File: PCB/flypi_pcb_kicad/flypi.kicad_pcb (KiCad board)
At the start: 2 copper layers, 76 x 93 mm, 44 parts, among them CON1 BARREL_JACK, P1 PeltS1S2, P10 RGB RG-B, P2 Pi+-, P3 Fan-+, P4 Therm +s-, P5 HP1-+, P6 HP2-+, P7 servo -s+, P8 Ring s-+, P9 matrix sdsc-+, Q1 1A_NPN_ECB, Q2 1A-NPN-ECB, Q3 1A_NPN_ECB, Q4 1A_NPN_ECB, U1 LM2596, U2 LM2596, U3 LM2596, U4 L298N, U5 arduino_mini

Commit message: same here.
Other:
- board text added: "Fly pi rev. 0.3 20170730"
- board text removed: "Fly pi rev. 0.2 20160726"
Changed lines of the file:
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@@
-(kicad_pcb (version 4) (host pcbnew 4.0.2+e4-6225~38~ubuntu14.04.1-stable)
+(kicad_pcb (version 4) (host pcbnew 4.0.6-e0-6349~53~ubuntu16.04.1)
   (general
     (links 94)
     (no_connects 3)
-    (area 102.4 38.4 187.7 136.55)
+    (area 102.4 38.4 187.55 136.55)
     (thickness 1.6)
     (drawings 11)
@@
       (excludeedgelayer true)
       (linewidth 0.100000)
-      (plotframeref false)
+      (plotframeref true)
       (viasonmask false)
       (mode 1)
@@
       (plotvalue true)
       (plotinvisibletext false)
-      (padsonsilk false)
+      (padsonsilk true)
       (subtractmaskfromsilk false)
       (outputformat 1)
@@
   (target plus (at 104.95 134.05) (size 5) (width 0.1) (layer Edge.Cuts))
   (target plus (at 181.05 134.05) (size 5) (width 0.1) (layer Edge.Cuts))
-  (gr_text "Fly pi rev. 0.2 20160726\n\n" (at 145.05 131.95) (layer F.SilkS)
+  (gr_text "Fly pi rev. 0.3 20170730\n\n" (at 145.05 131.95) (layer F.SilkS)
     (effects (font (size 1.5 1.5) (thickness 0.3)))
   )
@@
   (segment (start 116.16 76.84) (end 114.25 78.75) (width 0.5) (layer F.Cu) (net 2))
   (segment (start 113 87.5) (end 112 87.5) (width 0.5) (layer F.Cu) (net 2))
-  (segment (start 163 65) (end 163.25 65) (width 1) (layer B.Cu) (net 3) (status C00000))
-  (segment (start 163.25 65) (end 164.675 66.425) (width 1) (layer B.Cu) (net 3) (status 400000))
-  (segment (start 169.2 66.425) (end 171.725 63.9) (width 1) (layer B.Cu) (net 3) (status 800000))
+  (segment (start 163 65) (end 163.25 65) (width 1) (layer B.Cu) (net 3))
+  (segment (start 163.25 65) (end 164.675 66.425) (width 1) (layer B.Cu) (net 3))
+  (segment (start 169.2 66.425) (end 171.725 63.9) (width 1) (layer B.Cu) (net 3))
   (segment (start 164.675 66.425) (end 169.2 66.425) (width 1) (layer B.Cu) (net 3))
   (segment (start 171.775 62.925) (end 171.65 62.925) (width 1) (layer F.Cu) (net 3))
@@
   (segment (start 121 64.49936) (end 129.50064 64.49936) (width 1) (layer B.Cu) (net 4))
   (segment (start 129.50064 64.49936) (end 136 58) (width 1) (layer B.Cu) (net 4))
-  (segment (start 175.925 69) (end 175.925 68.725) (width 1) (layer F.Cu) (net 5) (status C00000))
-  (segment (start 175.925 68.725) (end 178.425 66.225) (width 1) (layer F.Cu) (net 5) (status 400000))
+  (segment (start 175.925 69) (end 175.925 68.725) (width 1) (layer F.Cu) (net 5))
+  (segment (start 175.925 68.725) (end 178.425 66.225) (width 1) (layer F.Cu) (net 5))
   (segment (start 173.4 52.35) (end 173.025 51.975) (width 1) (layer F.Cu) (net 5))
   (segment (start 176.65 52.35) (end 173.4 52.35) (width 1) (layer F.Cu) (net 5))
   (segment (start 178.425 54.125) (end 176.65 52.35) (width 1) (layer F.Cu) (net 5))
   (segment (start 178.425 66.225) (end 178.425 54.125) (width 1) (layer F.Cu) (net 5))
-  (segment (start 175.925 69) (end 175.925 75.25) (width 1) (layer F.Cu) (net 5) (status 400000))
+  (segment (start 175.925 69) (end 175.925 75.25) (width 1) (layer F.Cu) (net 5))
   (segment (start 175.925 75.25) (end 173.05 78.125) (width 1) (layer F.Cu) (net 5))
   (segment (start 173.1 79.125) (end 173.1 78.475) (width 1) (layer B.Cu) (net 5))

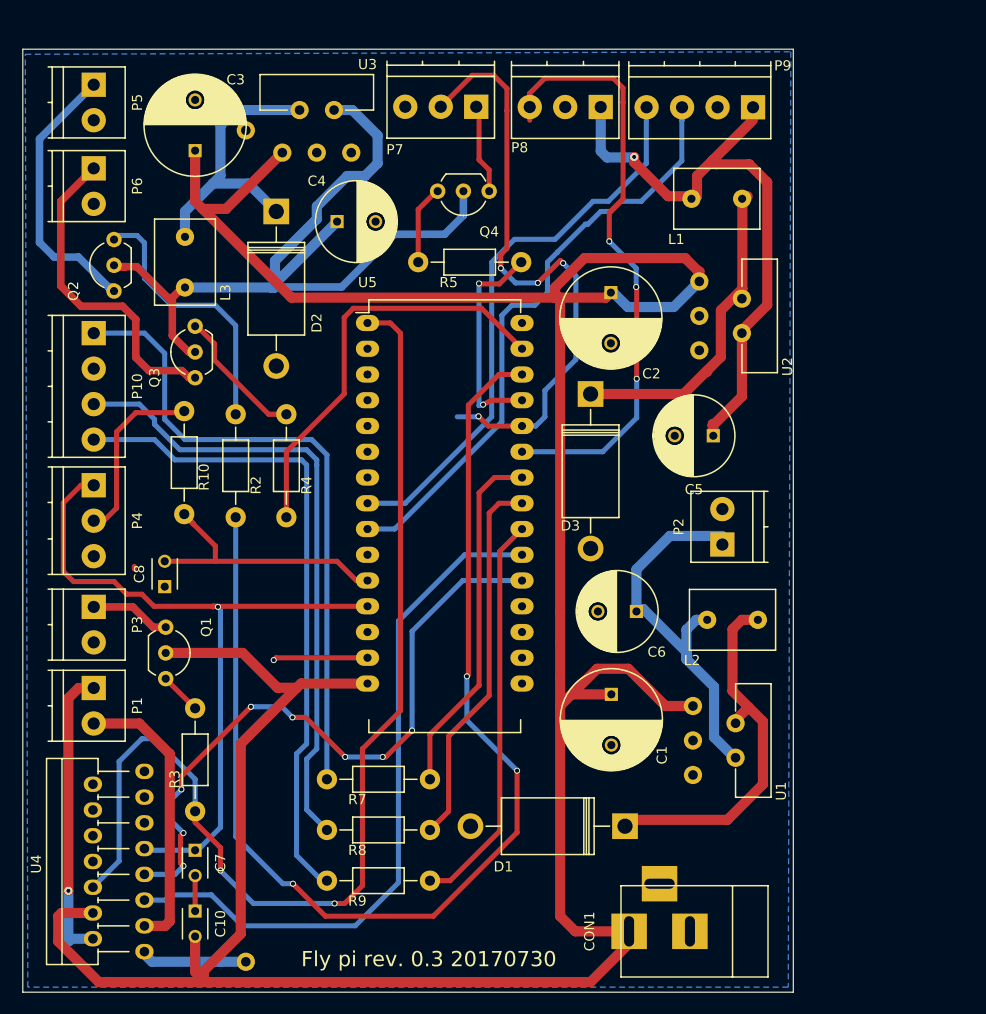
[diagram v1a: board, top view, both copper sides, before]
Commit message: update to pcbs. Both SMD and new through hole. PCB is untested.
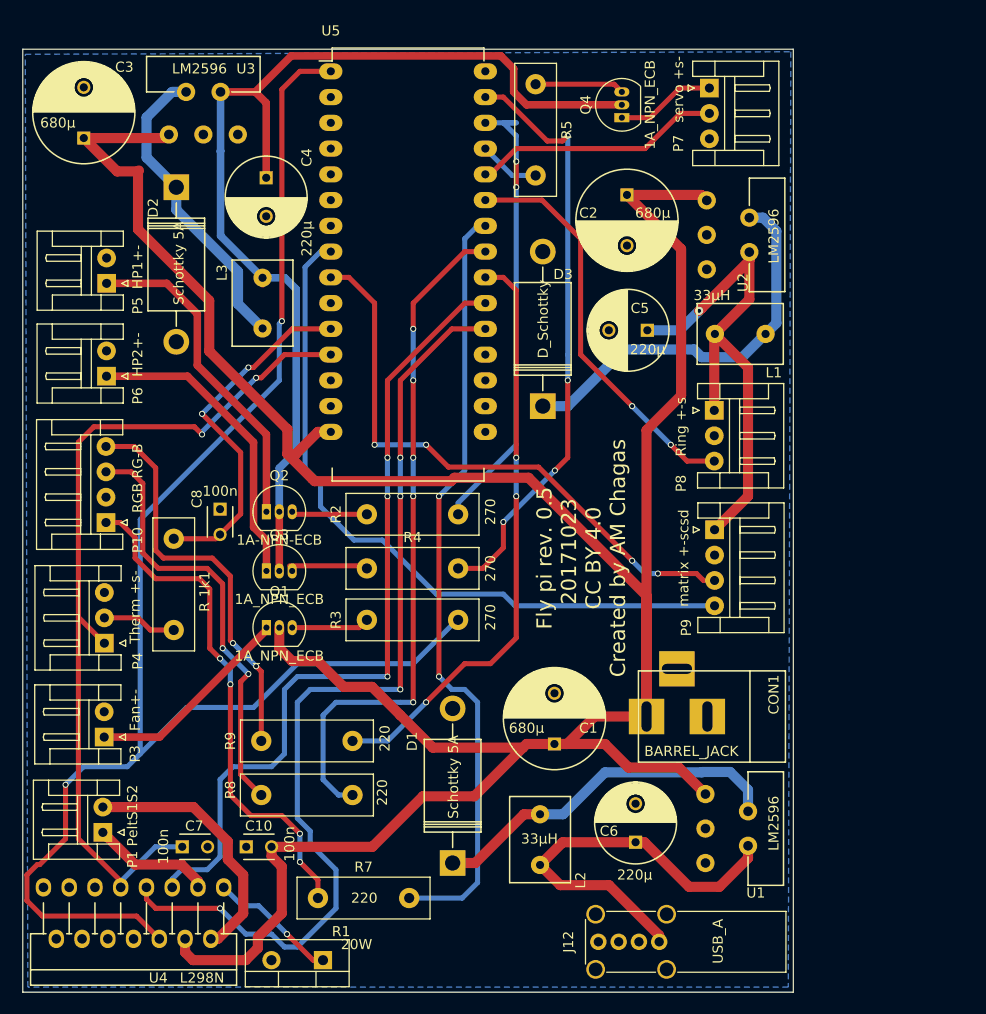
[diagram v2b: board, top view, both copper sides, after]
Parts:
- removed P2: Pi+-, Terminal_Blocks:TerminalBlock_Pheonix_PT-3.5mm_2pol
- removed R10: 1k, Resistors_ThroughHole:Resistor_Horizontal_RM10mm
- added 1k1: R, Resistors_THT:R_Box_L13.0mm_W4.0mm_P9.00mm, F.Cu at (119.9, 89.3)
- added J12: USB_A, Connectors:USB_A_Vertical, F.Cu at (167.8, 129.0)
- C8: value 0.1µ -> 100n
- P1: footprint Terminal_Blocks:TerminalBlock_Pheonix_PT-3.5mm_2pol -> Connectors_JST:JST_EH_S02B-EH_02x2.50mm_Angled
- P10: footprint Terminal_Blocks:TerminalBlock_Pheonix_PT-3.5mm_4pol -> Connectors_JST:JST_EH_S04B-EH_04x2.50mm_Angled
- P3: value Fan-+ -> Fan+-; footprint Terminal_Blocks:TerminalBlock_Pheonix_PT-3.5mm_2pol -> Connectors_JST:JST_EH_S02B-EH_02x2.50mm_Angled
- P4: footprint Terminal_Blocks:TerminalBlock_Pheonix_PT-3.5mm_3pol -> Connectors_JST:JST_EH_S03B-EH_03x2.50mm_Angled
- P5: value HP1-+ -> HP1+-; footprint Terminal_Blocks:TerminalBlock_Pheonix_PT-3.5mm_2pol -> Connectors_JST:JST_EH_S02B-EH_02x2.50mm_Angled
- P6: value HP2-+ -> HP2+-; footprint Terminal_Blocks:TerminalBlock_Pheonix_PT-3.5mm_2pol -> Connectors_JST:JST_EH_S02B-EH_02x2.50mm_Angled
- P7: value servo -s+ -> servo +s-; footprint Terminal_Blocks:TerminalBlock_Pheonix_PT-3.5mm_3pol -> Connectors_JST:JST_EH_S03B-EH_03x2.50mm_Angled
- P8: value Ring s-+ -> Ring +-s; footprint Terminal_Blocks:TerminalBlock_Pheonix_PT-3.5mm_3pol -> Connectors_JST:JST_EH_S03B-EH_03x2.50mm_Angled
- P9: value matrix sdsc-+ -> matrix +-scsd; footprint Terminal_Blocks:TerminalBlock_Pheonix_PT-3.5mm_4pol -> Connectors_JST:JST_EH_S04B-EH_04x2.50mm_Angled
- Q1, Q2, Q3, Q4: footprint TO_SOT_Packages_THT:TO-92_Inline_Wide -> TO_SOT_Packages_THT:TO-92_Inline_Narrow_Oval
- R1: value 1 - 18W -> 20W; footprint footprints:high_load_res -> TO_SOT_Packages_THT:TO-220-2_Vertical; moved to F.Cu
- R2, R3, R4, R5, R7, R8, R9: footprint Resistors_ThroughHole:Resistor_Horizontal_RM10mm -> Resistors_THT:R_Box_L13.0mm_W4.0mm_P9.00mm
- moved P9 41.8 mm to (173.2, 88.4), turned to 270 degrees
- moved R1 41.5 mm to (134.6, 130.8), turned to 180 degrees
- moved P8 31.9 mm to (173.2, 76.6), turned to 270 degrees
- moved L2 28.8 mm to (156.0, 119.0), turned to 270 degrees
- moved Q2 26.5 mm to (129.0, 86.6), turned to 0 degrees
- moved U5 25.1 mm to (135.4, 43.2)
- moved P7 23.1 mm to (172.7, 44.8), turned to 270 degrees
- moved C6 22.8 mm to (165.4, 119.2), turned to 90 degrees
- moved CON1 21.3 mm to (172.7, 106.8)
- moved R5 21.0 mm to (155.6, 44.5), turned to 270 degrees
- moved P6 20.5 mm to (113.3, 73.2), turned to 90 degrees
- moved Q3 20.3 mm to (129.0, 92.5), turned to 0 degrees
- moved P5 19.6 mm to (113.3, 64.1), turned to 90 degrees
- moved R3 19.0 mm to (138.9, 97.3), turned to 0 degrees
- moved P10 18.7 mm to (113.2, 87.7), turned to 90 degrees
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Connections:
- R1 pad 1: GND -> Net-(R1-Pad1)
- R1 pad 2: Net-(R1-Pad2) -> GND
- U4 pad 1: Net-(R1-Pad2) -> Net-(R1-Pad1)
- U4 pad 2: Net-(P1-Pad1) -> Net-(P1-Pad2)
- U4 pad 3: Net-(P1-Pad2) -> Net-(P1-Pad1)
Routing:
- net Net-(R2-Pad2): track 116.9 -> 46.2 mm, vias 3 -> 2
- net Net-(R7-Pad2): track 36.7 -> 76.8 mm, vias 0 -> 2
- net Net-(R3-Pad2): track 110.1 -> 150.1 mm
- net Net-(P7-Pad2): track 60.5 -> 25.3 mm, vias 4 -> 0
- net Net-(U4-Pad7): track 65.6 -> 98.2 mm, vias 8 -> 4
- net Net-(R8-Pad2): track 38.5 -> 68.5 mm, vias 0 -> 5
- net Net-(P10-Pad4): track 65.0 -> 39.8 mm, vias 0 -> 2
- net Net-(C4-Pad1): track 84.4 -> 106.3 mm
- net Net-(C1-Pad1): track 302.0 -> 280.4 mm
- net Net-(Q2-Pad3): track 27.6 -> 7.47 mm
- net Net-(P8-Pad3): track 59.6 -> 39.9 mm, vias 3 -> 2
- net Net-(P10-Pad3): track 62.3 -> 43.1 mm, vias 0 -> 2
- net Net-(R9-Pad2): track 40.2 -> 58.5 mm, vias 0 -> 3
- net Net-(P1-Pad1): track 29.4 -> 12.0 mm, vias 1 -> 0
- net Net-(R4-Pad2): track 41.6 -> 58.7 mm, vias 0 -> 4
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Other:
- board text added: "Fly pi rev. 0.5 20171023 CC BY 4.0 Created by AM Chagas"
- board text removed: "Fly pi rev. 0.3 20170730"

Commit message: change to gerber files
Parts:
- Q1, Q2, Q3: footprint TO_SOT_Packages_THT:TO-92_Inline_Narrow_Oval -> TO_SOT_Packages_THT:TO-92_Inline_Wide
- moved Q2 0.85 mm to (128.3, 87.0)
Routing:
- net Net-(C1-Pad1): track 280.4 -> 273.8 mm
- net Net-(Q1-Pad3): track 7.68 -> 5.14 mm
- net Net-(Q3-Pad3): track 7.73 -> 5.29 mm
- net Net-(P5-Pad1): track 32.5 -> 30.6 mm
- net Net-(Q2-Pad3): track 7.47 -> 5.64 mm
- net Net-(C4-Pad1): track 106.3 -> 105.3 mm
- net Net-(P6-Pad1): track 30.4 -> 30.1 mm, vias 0 -> 4
